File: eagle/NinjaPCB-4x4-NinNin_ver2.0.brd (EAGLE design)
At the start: 100 x 86 mm, 71 parts, among them IC3 ANALOGSW_AD_SOT23-6, IC6 NAU7802, J2 ATX24NH, J3 HEATER, J4 HEATER_TEMP, Q1 CJ2302, Q10 S9013, Q11 S9013, Q2 IRLB3813PBF, Q4 CJ2302, Q9 S9013, U1 CJT1117-3.3-SOT223

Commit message: wired
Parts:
- moved R3 92.4 mm to (31.4, 63.8), turned to 270 degrees
- moved R2 91.7 mm to (31.4, 67.4), turned to 90 degrees
- moved R7 78.3 mm to (43.9, 46.0)
- moved CP1 78.2 mm to (42.4, 71.4), turned to 180 degrees
- moved ESP1 76.6 mm to (56.4, 62.6)
- moved R14 71.6 mm to (63.3, 76.4), turned to 180 degrees
- moved ESP3 67.4 mm to (55.9, 36.8)
- moved R5 65.2 mm to (61.6, 76.4), turned to 180 degrees
- moved ESP2 64.5 mm to (49.0, 35.3)
- moved R1 64.2 mm to (65.1, 76.4)
- moved CP2 62.4 mm to (63.6, 46.6)
- moved R4 46.4 mm to (40.1, 17.8), turned to 180 degrees
- moved TP7 44.6 mm to (61.4, 9.00)
- moved R12 42.6 mm to (38.4, 17.8), turned to 180 degrees
- moved TP5 41.5 mm to (63.9, 9.00)
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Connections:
- net N$3: now also U$1.P$1
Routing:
- net GND: track 112.1 -> 484.6 mm, vias 0 -> 7
- net 3V3: track 0.00 -> 247.2 mm, vias 0 -> 4
- net HIGH_TEMP: track 0.00 -> 147.0 mm, vias 0 -> 2
- net RESET: track 0.00 -> 110.9 mm, vias 0 -> 2
- net PEL_SWA: track 0.00 -> 105.6 mm, vias 0 -> 3
- net FAN: track 0.00 -> 102.3 mm, vias 0 -> 4
- net N$3: track 0.00 -> 99.2 mm, vias 0 -> 6
- net RXD: track 0.00 -> 98.1 mm, vias 0 -> 2
- net 12V: track 82.4 -> 178.6 mm
- net TXD: track 0.00 -> 95.1 mm, vias 0 -> 2
- net MODE: track 0.00 -> 89.3 mm, vias 0 -> 4
- net DRDY: track 0.00 -> 87.7 mm, vias 0 -> 4
- net PEL_PWM: track 0.00 -> 78.6 mm, vias 0 -> 2
- net HEATER: track 0.00 -> 71.5 mm, vias 0 -> 3
- net PEL_SWB: track 0.00 -> 63.4 mm, vias 0 -> 1
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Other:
- board size 100 x 86 mm -> 70 x 86 mm

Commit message: dru clear
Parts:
- moved TP1 10.6 mm to (48.3, 1.78)
- moved R12 10.3 mm to (34.0, 27.2), turned to 90 degrees
- moved R18 10.2 mm to (34.0, 43.9)
- moved R20 10.2 mm to (34.0, 42.2)
- moved Q11 10.2 mm to (34.0, 39.5)
- moved R17 10.2 mm to (34.0, 30.7)
- moved R13 10.2 mm to (34.0, 34.1)
- moved R15 10.2 mm to (34.0, 28.9)
- moved R16 10.2 mm to (34.0, 32.3)
- moved R19 10.2 mm to (34.0, 36.8)
- moved R7 9.86 mm to (34.0, 45.7), turned to 90 degrees
- moved R9 9.76 mm to (34.0, 23.6), turned to 270 degrees
- moved R4 9.70 mm to (34.0, 25.4), turned to 90 degrees
- moved R1 7.85 mm to (58.0, 73.2), turned to 270 degrees
- moved C2 7.76 mm to (34.5, 20.0), turned to 180 degrees
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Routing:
- net GND: track 484.6 -> 519.1 mm, vias 7 -> 9
- net FAN: track 102.3 -> 124.7 mm
- net 3V3: track 247.2 -> 260.9 mm, vias 4 -> 3
- net PEL_PWM: track 78.6 -> 66.8 mm
- net TXD: track 95.1 -> 106.7 mm
- net HEATER_TEMP: track 31.5 -> 42.5 mm
- net N$32: track 7.26 -> 17.4 mm
- net N$8: track 7.26 -> 16.8 mm
- net N$1: track 10.8 -> 18.0 mm
- net RESET: track 110.9 -> 117.8 mm
- net SCLK: track 57.9 -> 64.4 mm
- net PEL_SWA: track 105.6 -> 111.2 mm
- net N$27: track 9.90 -> 4.38 mm
- net SDIO: track 53.8 -> 59.2 mm
- net HEATER: track 71.5 -> 66.2 mm
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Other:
- board size 70 x 86 mm -> 63 x 86 mm

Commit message: minor tunes
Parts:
- moved Q10 1.27 mm to (34.0, 57.4)
- moved R2 1.27 mm to (34.0, 63.6)
- moved R22 1.27 mm to (34.0, 61.8)
- moved R3 1.27 mm to (34.0, 60.0)
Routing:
- net PEL_SWA: track 111.2 -> 109.9 mm
- net PEL_SWB: track 59.7 -> 58.4 mm
- net SDIO: track 59.2 -> 58.1 mm
- net 3V3: track 260.9 -> 260.3 mm
- net N$36: track 9.24 -> 9.77 mm

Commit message: ready to order
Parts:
- removed C7: CAP_SMDAL_1000UF_25V, Seeed-OPL-2017-01-Capacitor-akita:CAP_SMD_AL_D125
- removed ESP3: ESP-WROOM-02-BREAK, PCR-Module:ESP-WROOM-02-BREAK
- removed Q9: S9013, Seeed-Transistor:SOT-23
- removed R19, R20: 10K 1/10W, Seeed-Resistor:R0603
- added C1: 100nf, Seeed-Capacitor:C0603
- added ESP-WROOM-02-BREAK: ESP-WROOM-02-BREAKND, PCR-Module:ESP-WROOM-02-BREAK-NODETAIL
- added HEATSINK: HEAT111PB015, PCR-Connector:HEAT11PB015
- added Q3: CJ2302, Seeed-Transistor:SOT-23
- added R6, R8: 10K 1/10W, Seeed-Resistor:R0603
- added U$2: (no value), PCR-Logo:TORI_0.25
- C3: value 100nf -> CAP_SMDAL_1000UF_25V; device Seeed-Capacitor:C0603 -> Seeed-OPL-2017-01-Capacitor-akita:CAP_SMD_AL_D125
- HEATER_POWER: value HEATER -> (none)
- HEATER_TEMP: value HEATER_TEMP -> (none)
- Q1: value CJ2302 -> IRLB3813PBF; device Seeed-Transistor:SOT-23 -> transistor-power:TO220BV
- Q2: value IRLB3813PBF -> CJ2302; device transistor-power:TO220BV -> Seeed-Transistor:SOT-23
- Q4: value CJ2302 -> S9013
- R12, R17: value 10K 1/10W -> 1K 1/10W
- R16, R18: value 1K 1/10W -> 10K 1/10W
- U$1: value HEAT111PB015 -> (none); device PCR-Connector:HEAT11PB015 -> PCR-Logo:TORI_0.25
- moved C3 68.1 mm to (28.8, 10.1)
- moved C2 58.7 mm to (42.9, 78.1), turned to 270 degrees
- moved C4 58.7 mm to (34.5, 20.0), turned to 180 degrees
- moved Q4 57.9 mm to (6.74, 74.2), turned to 180 degrees
- moved R9 56.7 mm to (58.0, 74.9), turned to 90 degrees
- moved R1 55.0 mm to (34.0, 23.6)
- moved R4 53.4 mm to (58.0, 73.2), turned to 270 degrees
- moved R14 40.6 mm to (34.0, 42.2), turned to 270 degrees
- moved U$1 39.1 mm to (6.10, 0.28), turned to 0 degrees
- moved R2 38.2 mm to (34.0, 25.4)
- moved R3 29.2 mm to (58.0, 76.7), turned to 90 degrees
- moved R5 27.3 mm to (34.0, 63.6)
- moved R12 16.8 mm to (34.0, 43.9), turned to 270 degrees
- moved Q1 13.6 mm to (22.1, 36.0), turned to 270 degrees
- moved Q2 13.6 mm to (26.4, 23.0), turned to 90 degrees
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- renumbered ESP1 to ESP-12, ESP2 to ESP-WROOM-02, IC3 to IC1, IC6 to IC2, J2 to ATX, J3 to HEATER_POWER, J4 to HEATER_TEMP, JP2 to FAN, Q10 to Q5, Q11 to Q6, R21 to R10, R22 to R11, TP1 to T1, TP2 to T2, TP3 to T3, TP4 to T4, TP5 to T5, TP6 to T6, TP7 to T7, U1 to REG
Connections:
- net 12V: now also C3.P$P, R13.2; no longer C7.P$P, R19.2
- net 3V3: now also C4.+, ESP-WROOM-02-BREAK.P$1, R2.1, R3.1; no longer C2.+, ESP3.P$1, R5.1, R9.1
- net DIVIDED: now also C2.+; no longer C4.+
- net DRDY: now also ESP-WROOM-02-BREAK.P$14; no longer ESP3.P$14
- net EN: now also ESP-WROOM-02-BREAK.P$2, R4.2; no longer ESP3.P$2, R1.2
- net FAN: now also ESP-WROOM-02-BREAK.P$8, R17.1, R2.2; no longer ESP3.P$8, R15.1, R4.2
- net GND: now also C1.1, C3.P$M, ESP-WROOM-02-BREAK.P$13, ESP-WROOM-02-BREAK.P$18, ESP-WROOM-02-BREAK.P$9, Q1.S, Q2.2, Q3.2, R16.1, R18.1, R5.1, R6.1, R8.1, R9.1; no longer C3.1, C7.P$M, ESP3.P$13, ESP3.P$18, ESP3.P$9, Q1.2, Q2.S, Q9.2, R12.1, R13.1, R17.1, R2.1, R20.1, R3.1
- net HEATER: now also ESP-WROOM-02-BREAK.P$6, R15.1; no longer ESP3.P$6, R16.1
- net HIGH_TEMP: now also ESP-WROOM-02-BREAK.P$17, R8.2; no longer ESP3.P$17, R12.2
- net MODE: now also ESP-WROOM-02-BREAK.P$16, R9.2; no longer ESP3.P$16, R14.2
- net N$2: now also Q2.3; no longer Q1.3
- net N$3: now also HEATSINK.P$1, Q1.D; no longer Q2.D, U$1.P$1
- net N$30: now also R12.2; no longer R18.2
- net N$32: now also Q2.1, R15.2; no longer Q1.1, R13.2
- net N$33: now also Q4.3; no longer Q9.3
- net N$34: now also Q4.1; no longer Q9.1
- net N$4: now also Q3.3; no longer Q4.3
- net N$5: now also Q1.G, R13.1, R14.2; no longer Q2.G, R19.1, R20.2
- net N$8: now also Q3.1, R18.2; no longer Q4.1, R15.2
- net N$92: now also C1.2; no longer C3.2
- net PEL_PWM: now also ESP-WROOM-02-BREAK.P$10, R12.1; no longer ESP3.P$10, R18.1
- net PEL_SWA: now also ESP-WROOM-02-BREAK.P$4, R5.2; no longer ESP3.P$4, R2.2
- net PEL_SWB: now also ESP-WROOM-02-BREAK.P$5, R6.2; no longer ESP3.P$5, R3.2
- net RESET: now also ESP-WROOM-02-BREAK.P$15, R1.2; no longer ESP3.P$15, R9.2
- net RXD: now also ESP-WROOM-02-BREAK.P$11; no longer ESP3.P$11
- net SCLK: now also ESP-WROOM-02-BREAK.P$3; no longer ESP3.P$3
- net SDIO: now also ESP-WROOM-02-BREAK.P$7, R3.2; no longer ESP3.P$7, R5.2
- net TXD: now also ESP-WROOM-02-BREAK.P$12; no longer ESP3.P$12
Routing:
- net GND: track 518.8 -> 790.9 mm, vias 9 -> 41
- net PEL_SWB: track 58.4 -> 65.7 mm
- net PEL_SWA: track 109.9 -> 116.6 mm
- net FAN: track 124.7 -> 118.4 mm
- net HIGH_TEMP: track 147.6 -> 143.6 mm
- net HEATER: track 66.2 -> 62.6 mm
- net SCLK: track 64.4 -> 67.2 mm
- net 3V3: track 260.3 -> 262.7 mm
- net RESET: track 117.8 -> 119.4 mm
- net DRDY: track 88.5 -> 89.6 mm
- net TXD: track 106.7 -> 107.6 mm
- added copper zone on layer 1, net GND
- added copper zone on layer 16, net GND
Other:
- board text added: "*"
- board text added: "+"
- board text added: "63x86mm"
- board text added: "ATX"
- board text added: "C1"
- board text added: "C2"
- board text added: "C3"
- board text added: "C4"
- board text added: "CP1"
- board text added: "CP2"
- board text added: "D1"
- board text added: "D2"
- board text added: "ESP-12"
- board text added: "ESP-WROOM-02"
- board text added: "FAN"
- board text added: "HEATER POWER"
- board text added: "HEATER TEMP"
- board text added: "HEATSINK"
- board text added: "IC1"
- board text added: "IC2"
- board text added: "IO0"
- board text added: "MODE"
- board text added: "NinjaPCB-4x4-NinNin ver2.0"
- board text added: "ON"
- board text added: "PEL BLK"
- board text added: "PEL RED"
- board text added: "Q1"
- board text added: "Q2"
- board text added: "Q3"
- board text added: "Q4"
- board text added: "Q5"
- board text added: "Q6"
- board text added: "R1"
- board text added: "R10"
- board text added: "R11"
- board text added: "R12"
- board text added: "R13"
- board text added: "R14"
- board text added: "R15"
- board text added: "R16"
- board text added: "R17"
- board text added: "R18"
- board text added: "R2"
- board text added: "R3"
- board text added: "R4"
- board text added: "R5"
- board text added: "R6"
- board text added: "R7"
- board text added: "R8"
- board text added: "R9"
- board text added: "RD1"
- board text added: "RD2"
- board text added: "REG"
- board text added: "RELAY"
- board text added: "RH"
- board text added: "RL1"
- board text added: "RL2"
- board text added: "RST"
- board text added: "RT"
- board text added: "SERIAL4"
- board text added: "SERIAL6"
- board text added: "T1"
- board text added: "T2"
- board text added: "T3"
- board text added: "T4"
- board text added: "T5"
- board text added: "T6"
- board text added: "T7"
- board text added: "WELL_TEMP"
- board text added: "https://github.com/hisashin/NinjaPCR"

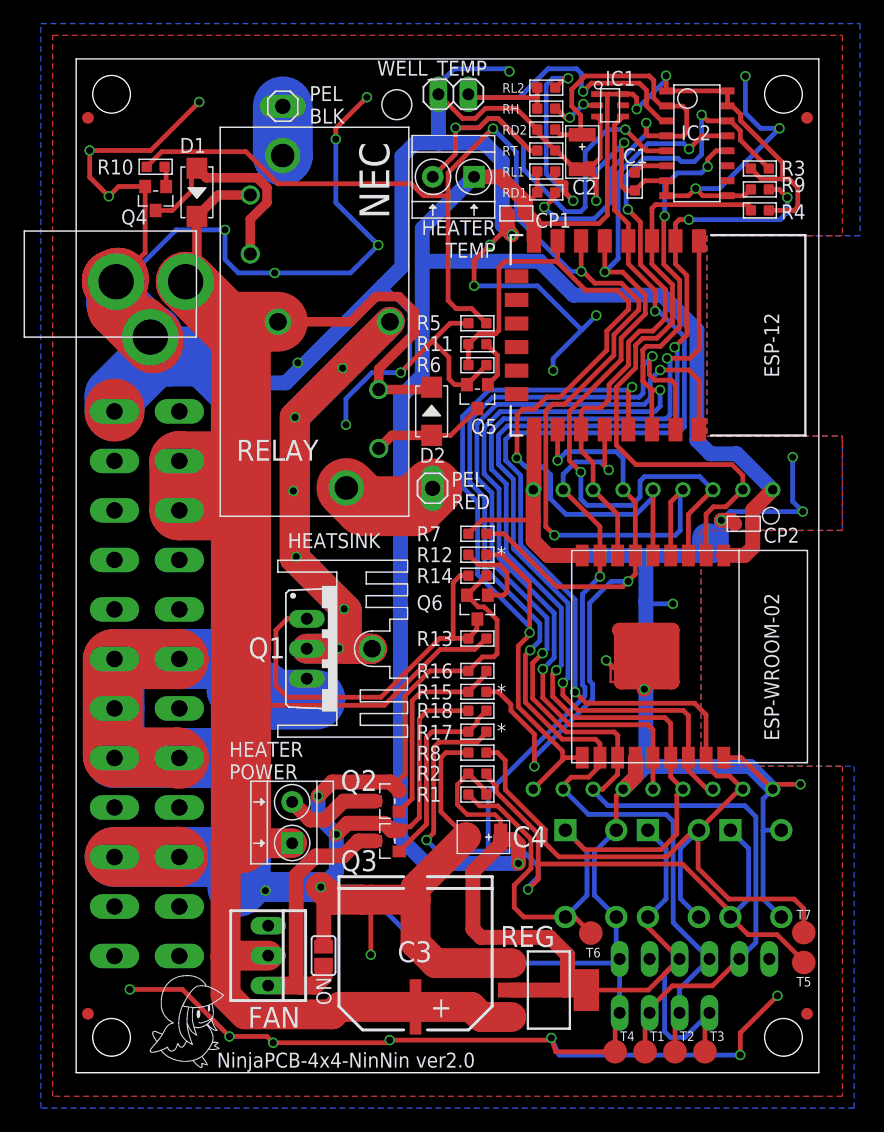
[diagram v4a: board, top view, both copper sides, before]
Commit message: panelized NinNin
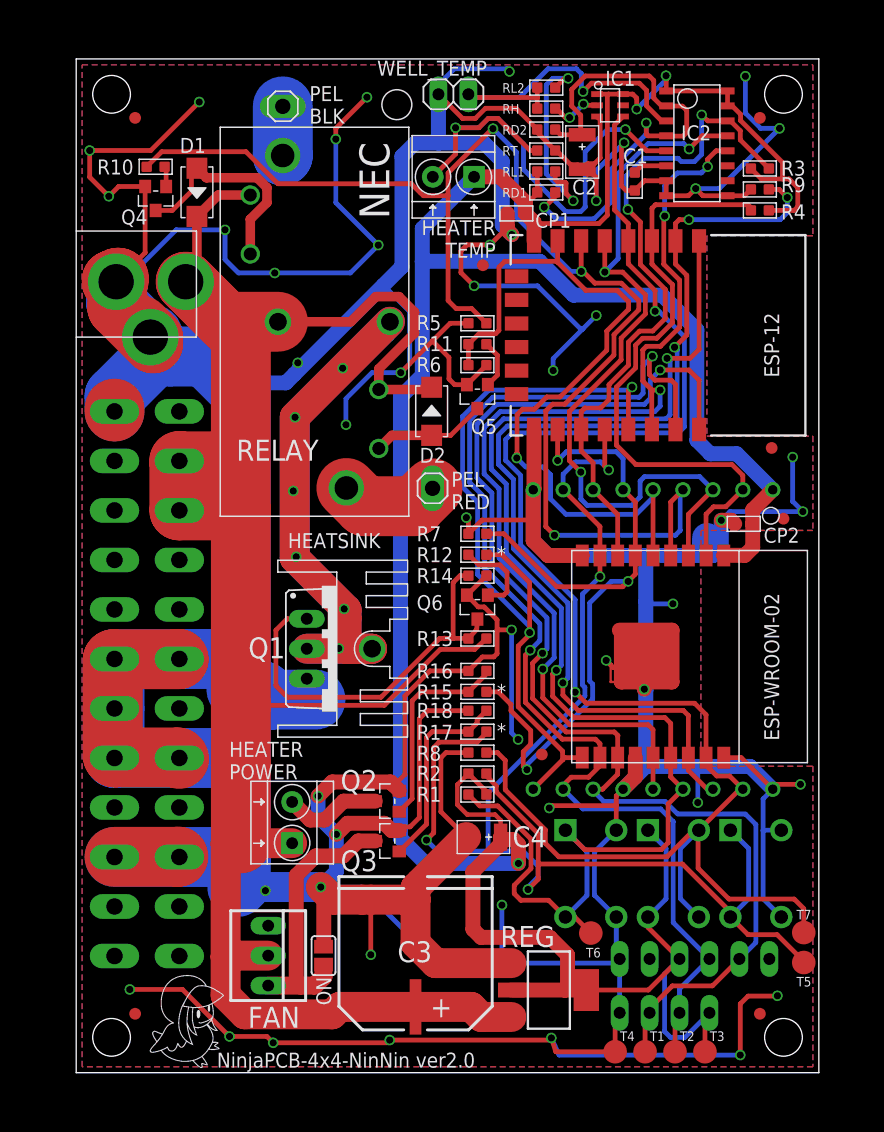
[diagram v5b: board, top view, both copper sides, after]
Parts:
- added U$10, U$7, U$8, U$9: FIDUCIAL, adafruit:FIDUCIAL_1MM
- JACK: value 2.1MMJACKTHM -> 2.1MMJACKTHM-NOOUT; device adafruit:PJ-102A -> adafruit:PJ-102A-NOOUT
- moved U$3 4.00 mm to (58.0, 5.00)
- moved U$4 4.00 mm to (58.0, 81.0)
- moved U$5 4.00 mm to (5.00, 5.00)
- moved U$6 4.00 mm to (5.00, 81.0)
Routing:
- net GND: track 790.9 -> 823.1 mm, vias 41 -> 47
- net HEATER: track 62.6 -> 63.6 mm
- net RESET: track 119.4 -> 118.7 mm
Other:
- board text added: "63 x 86 mm"
- board text removed: "63x86mm"

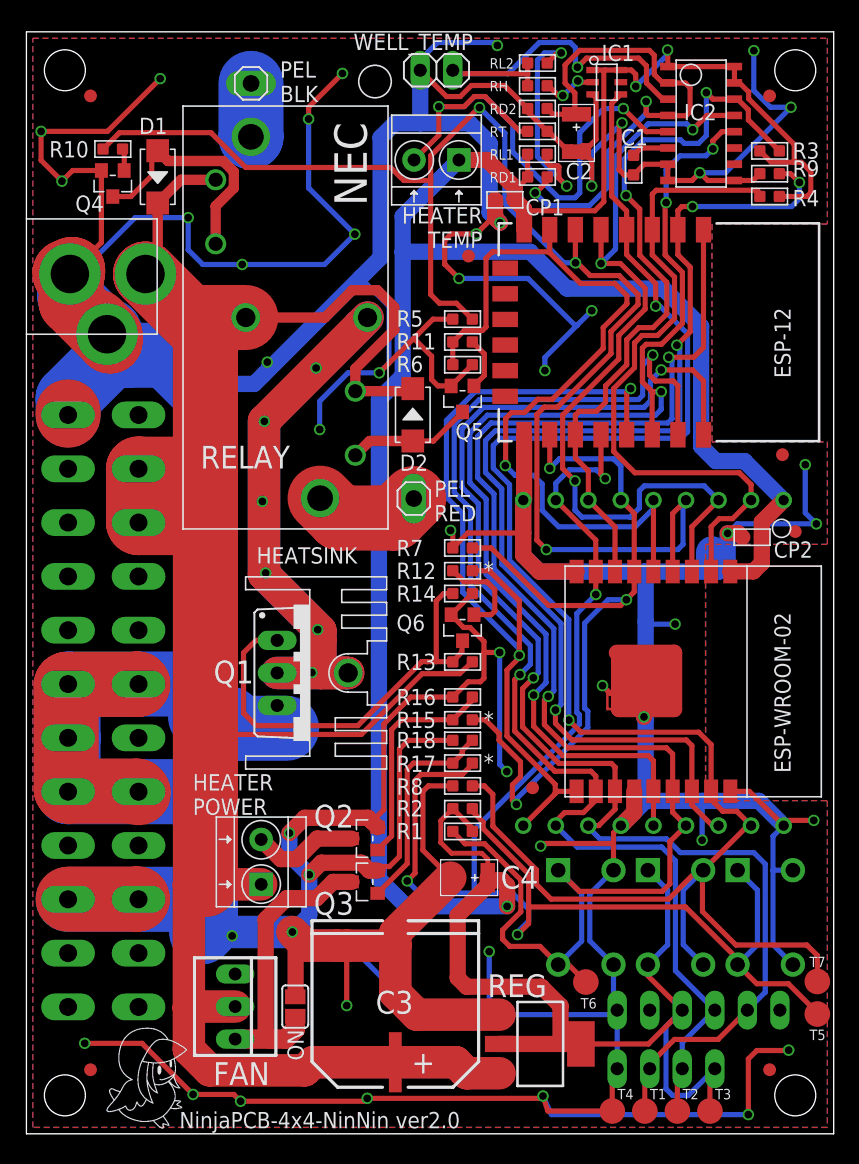
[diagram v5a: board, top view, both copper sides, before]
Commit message: set distance more equal 10mil for 2oz at Seeed
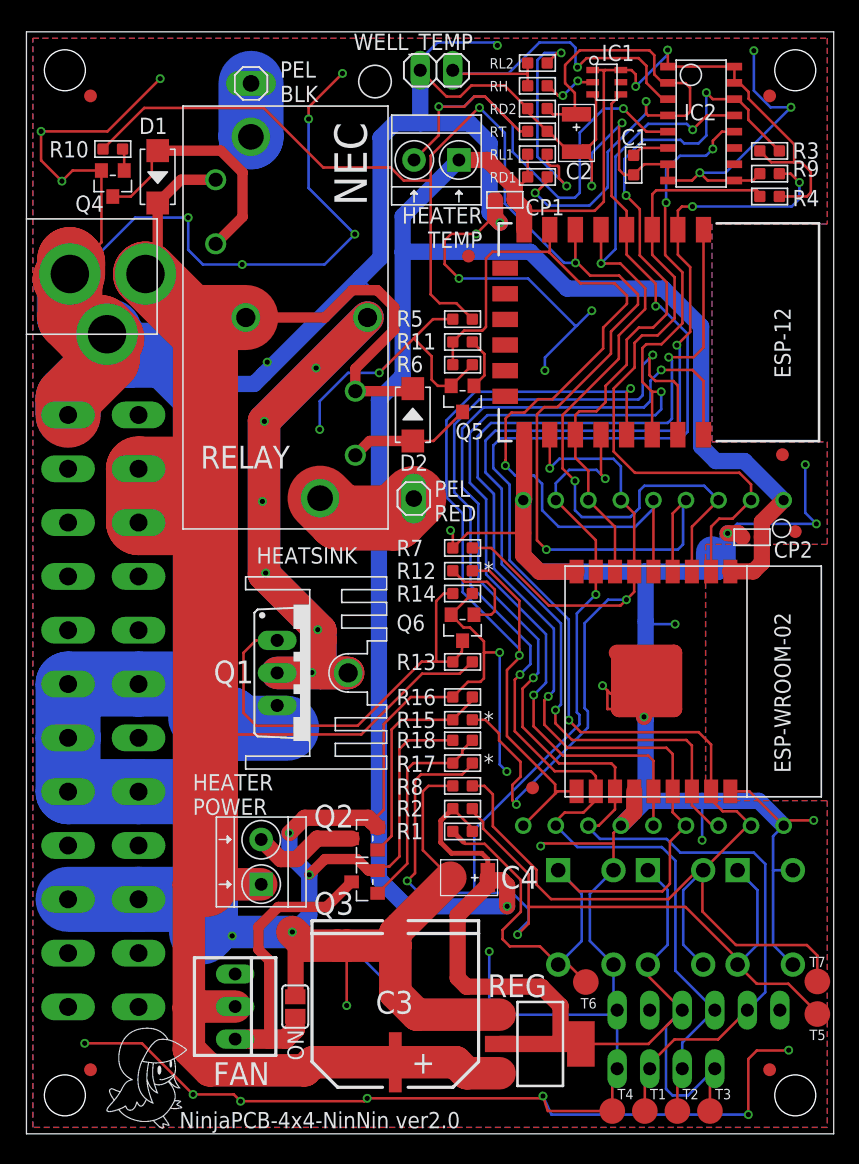
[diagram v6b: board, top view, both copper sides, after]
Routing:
- net GND: track 823.1 -> 809.8 mm
- net PEL_SWA: track 116.6 -> 118.2 mm
- net N$33: track 18.7 -> 19.6 mm
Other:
- board outline removed
